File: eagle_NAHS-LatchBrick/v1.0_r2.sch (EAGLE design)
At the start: 39 parts, among them IC1 ESP12F, IC2 ATTINY212-SSNR, IC3 TP4056, IC4 DW01A, IC5 FT232RL, J1 10118194-0001LF, Q1 8205A

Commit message: saving
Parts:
- removed C1, C3: 100nF, rcl:C-EUC0805
- removed IC5: FT232RL, ftdichip:FT232RL
- added J2: Brick-Interface, no_molex:NAHS-BRICK-INTERFACE_B-SIDE
- added R14: 10k, rcl:R-EU_R0805
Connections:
- removed net VCCIO: C3.1, IC5.3V3OUT, IC5.VCCIO
- new net CD: IC3.CE, J2.CD, R14.2
- net +3V3: now also J2.3.3V
- net D+: now also J2.D+; no longer IC5.USBDP
- net D-: now also J2.D-; no longer IC5.USBDM
- net IN+: now also J2.5V; no longer C1.1, IC5.VCC
- net IN-: now also J2.GND; no longer C1.2, C3.2, IC5.GND, IC5.GND@1, IC5.GND@2, IC5.GND@A, IC5.TEST
- net N$1: now also R14.1; no longer IC3.CE
- net PROG: now also J2.PROG
- net RXD: now also J2.RX; no longer IC5.TXD
- net SETUP: now also J2.SETUP
- net TXD: now also J2.TX; no longer IC5.RXD
- net UPDI: now also J2.UPDI1
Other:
- moved on the sheet: BT1, C6, IC1, IC2, IC3, J1, JP1_1, JP1_2, JP1_3, JP1_4, JP2_1, JP2_2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

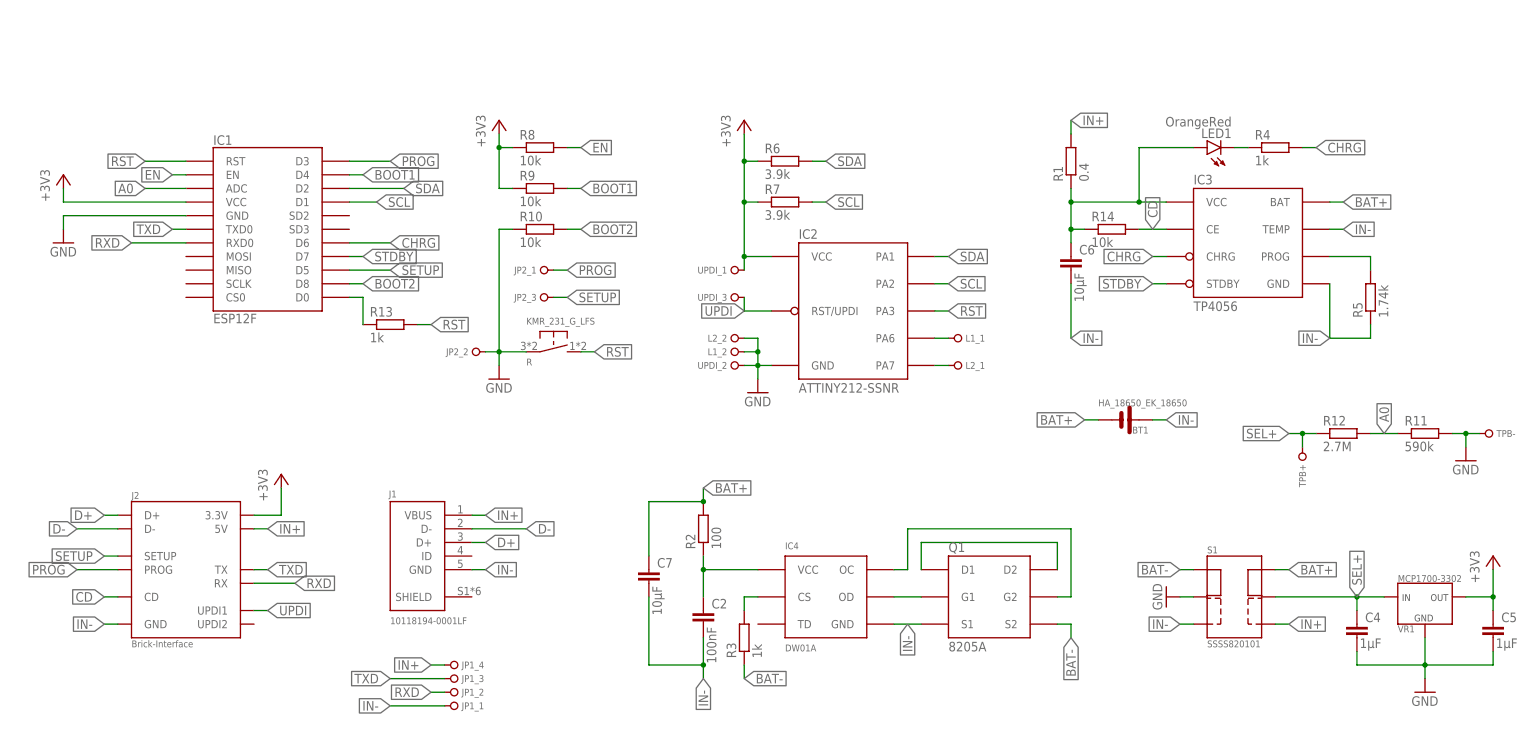
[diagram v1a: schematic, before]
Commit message: komponenten mit kleineren bohrungen eingesetzt
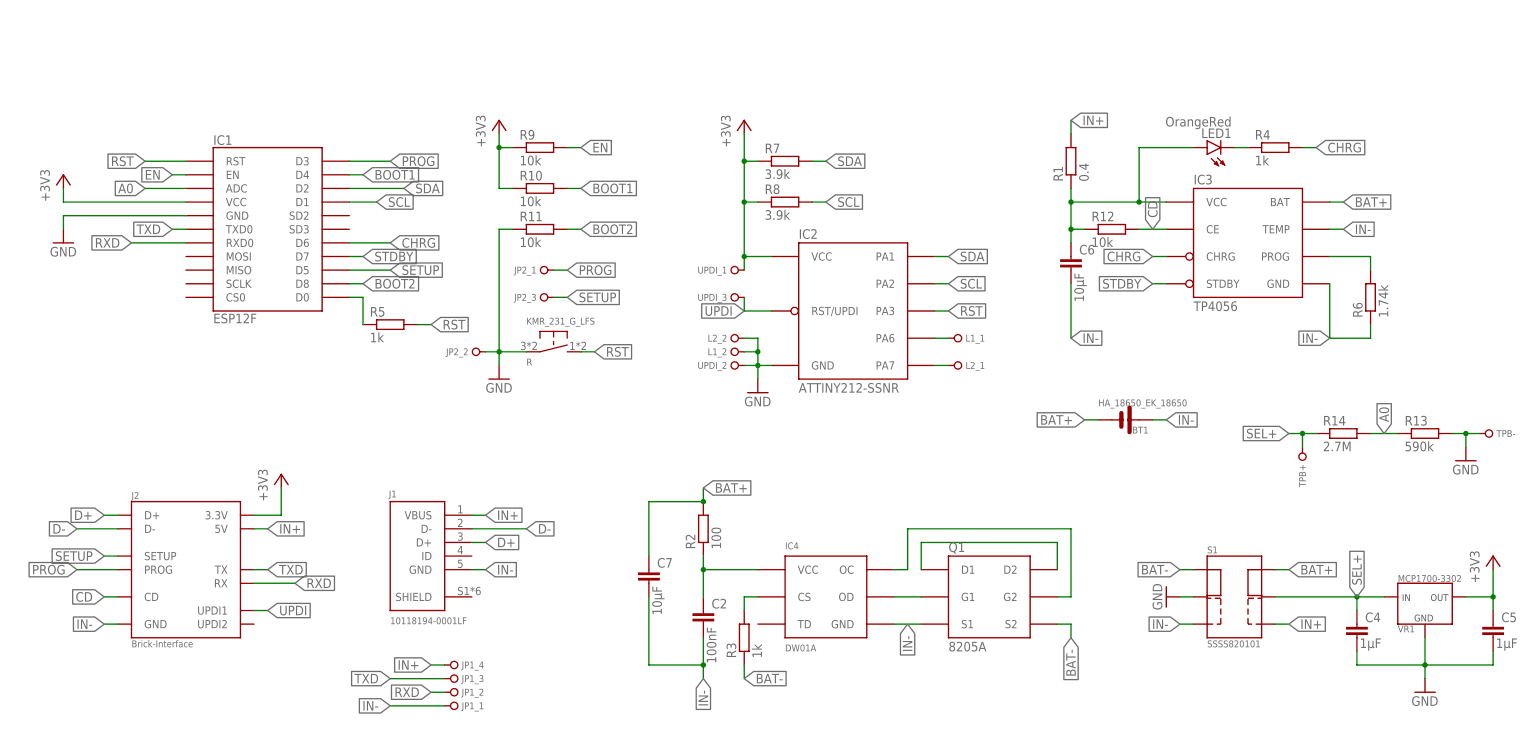
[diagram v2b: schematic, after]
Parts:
- R11: value 590k -> 10k
- R12: value 2.7M -> 10k
- R13: value 1k -> 590k
- R14: value 10k -> 2.7M
- R5: value 1.74k -> 1k
- R6: value 3.9k -> 1.74k
- R8: value 10k -> 3.9k
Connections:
- net +3V3: now also R10.1; no longer R6.1
- net A0: now also R13.1, R14.2; no longer R11.1, R12.2
- net BOOT1: now also R10.2; no longer R9.2
- net BOOT2: now also R11.2; no longer R10.2
- net CD: now also R12.2; no longer R14.2
- net EN: now also R9.2; no longer R8.2
- net GND: now also R11.1, R13.2; no longer R10.1, R11.2
- net IN-: now also R6.1; no longer R5.1
- net N$1: now also R12.1; no longer R14.1
- net N$2: now also R6.2; no longer R5.2
- net RST: now also R5.2; no longer R13.2
- net SCL: now also R8.2; no longer R7.2
- net SDA: now also R7.2; no longer R6.2
- net SEL+: now also R14.1; no longer R12.1
- net WAKE: now also R5.1; no longer R13.1
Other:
- moved on the sheet: R10, R11, R12, R13, R14, R5, R6, R7, R8, R9
